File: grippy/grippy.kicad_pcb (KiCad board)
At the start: 2 copper layers, 60.8 x 35.2 mm, 9 parts, among them J1 Conn_01x08_Socket, SW0 SW_SPST, SW1 SW_SPST, SW2 SW_SPST, SW3 SW_SPST, SW4 SW_SPST, SW5 SW_DPDT_x2, U1 esp32s3-supermini

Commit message: general updates
ready to cut another pcb
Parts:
- moved BAT1 0.33 mm to (180.5, 95.0), turned to 0 degrees
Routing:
- net /B+: track 14.3 -> 12.1 mm
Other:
- board text added: "20251202"
- board text added: "blk"
- board text added: "cs"
- board text added: "dc"
- board text added: "gnd"
- board text added: "res"
- board text added: "scl"
- board text added: "sda"
- board text added: "vcc"
- board text removed: "20251018"
- board text removed: "BAT 150mah 401730"
- board text removed: "BAT 220mAh 751424"

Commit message: cut-out for new supermini
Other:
- board text added: "20251216"
- board text removed: "20251202"

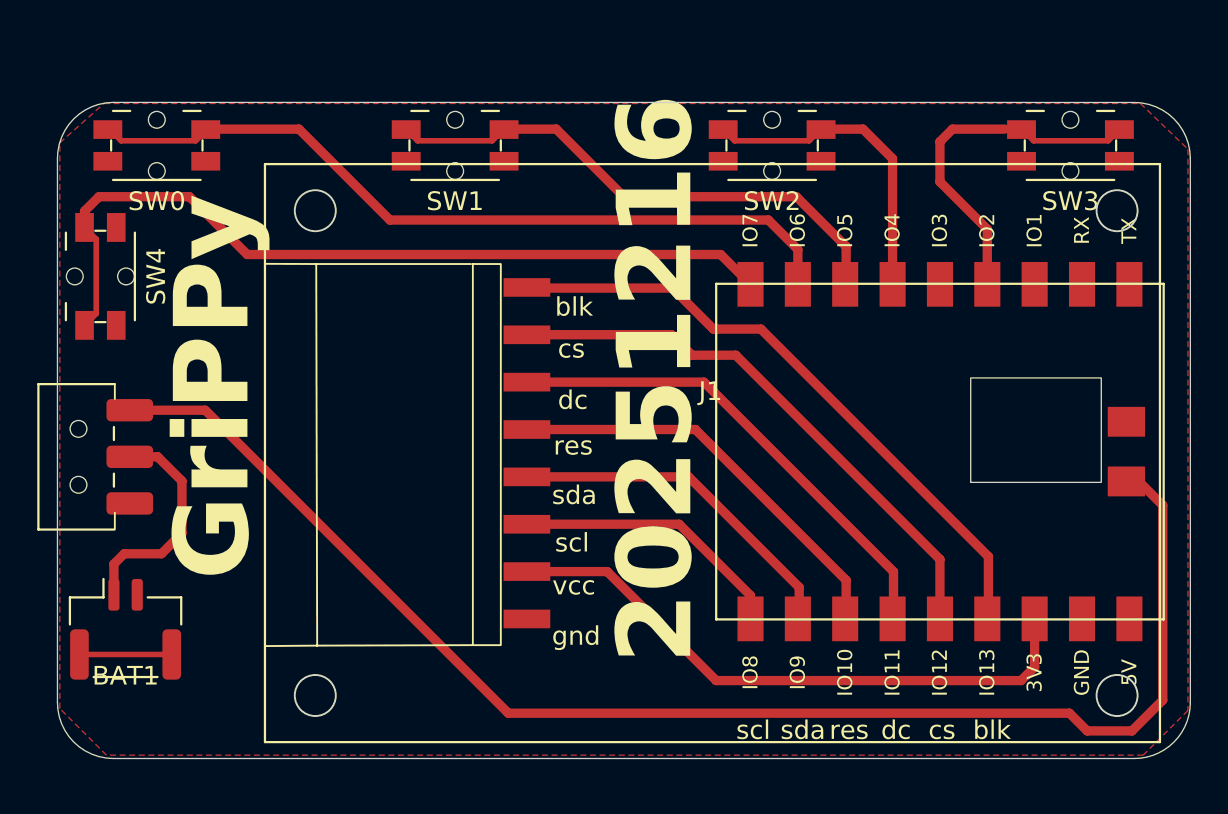
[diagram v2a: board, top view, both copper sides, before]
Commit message: moved battery receptacle
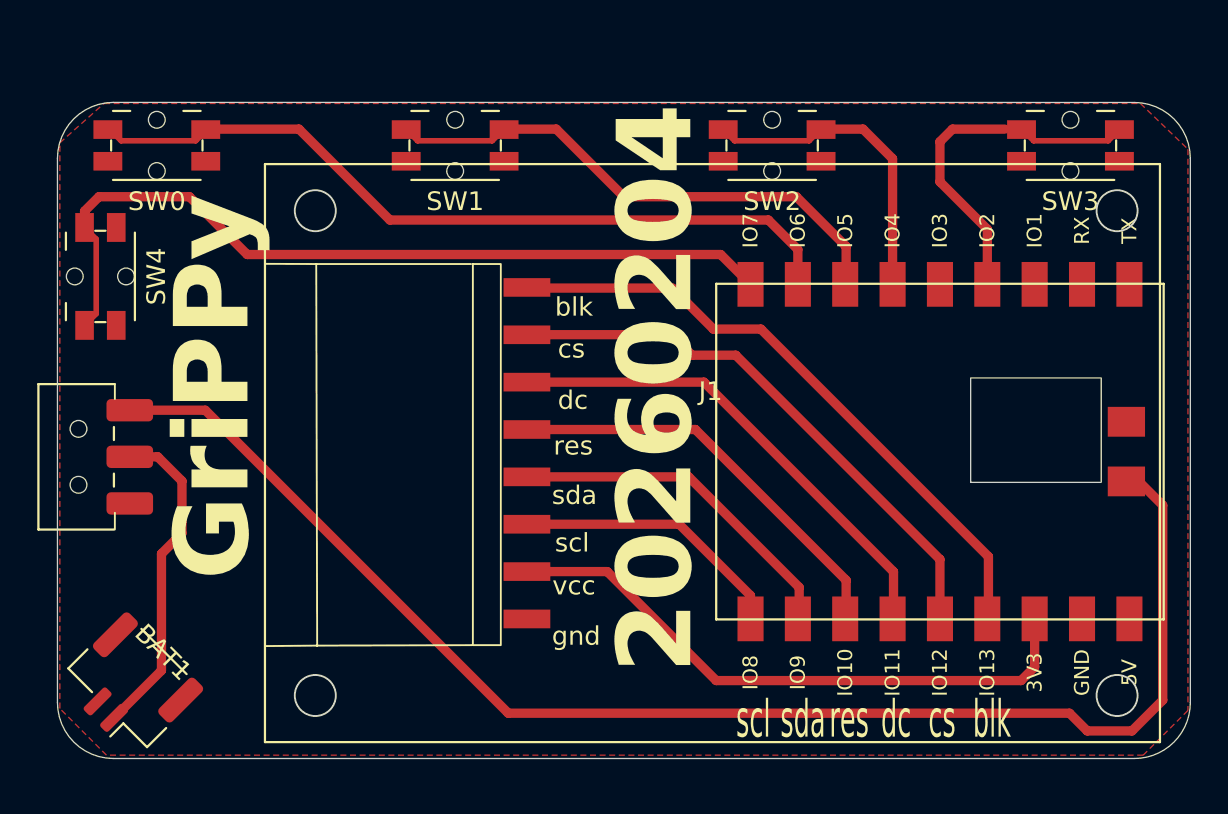
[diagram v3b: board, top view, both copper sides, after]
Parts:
- moved BAT1 3.01 mm to (180.8, 98.0), turned to 135 degrees
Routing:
- net /B+: track 12.1 -> 17.5 mm
- net /mp: track 4.95 -> 0.00 mm
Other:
- board text added: "20260204"
- board text added: "Grippy 20260204"
- board text removed: "20251216"

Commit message: wider
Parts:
- moved SW4 0.10 mm to (179.3, 76.0)
- moved SW0 0.08 mm to (182.2, 69.1)
- moved SW1 0.08 mm to (198.2, 69.1)
- moved SW2 0.08 mm to (215.2, 69.1)
- moved SW3 0.08 mm to (231.2, 69.1)
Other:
- board text added: "20260308"
- board text added: "Grippy 20260308"
- board text removed: "20260204"
- board text removed: "Grippy 20260204"
